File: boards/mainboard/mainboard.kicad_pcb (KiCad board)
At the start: 2 copper layers, 316.2 x 120.7 mm, 278 parts, among them J101 Powerboard <-> Mainboard, J102 Temperature & Pressure, J103 Camera board, J201 RTD_31-36, P901 DEBUG, P902 SWD, SW101 SW_PUSH, SW102 SW_PUSH, SW901 RESET, SW902 BOOT0, U1001 SST26VF064B, U101 LM1117-3.3, U1101 SST26VF064B, U1201 Heat probe encoder, U1202 DS26LV32AT, U1203 DS26LV32AT, U201 RTD_20-30, U202 RTD_1-19, U301 LTC2984, U401 LTC2984, U501 LTC2984, U601 LTC2984, U701 LTC2984, U801 LTC2984, U901 STM32F429ZITx, X901 XO53

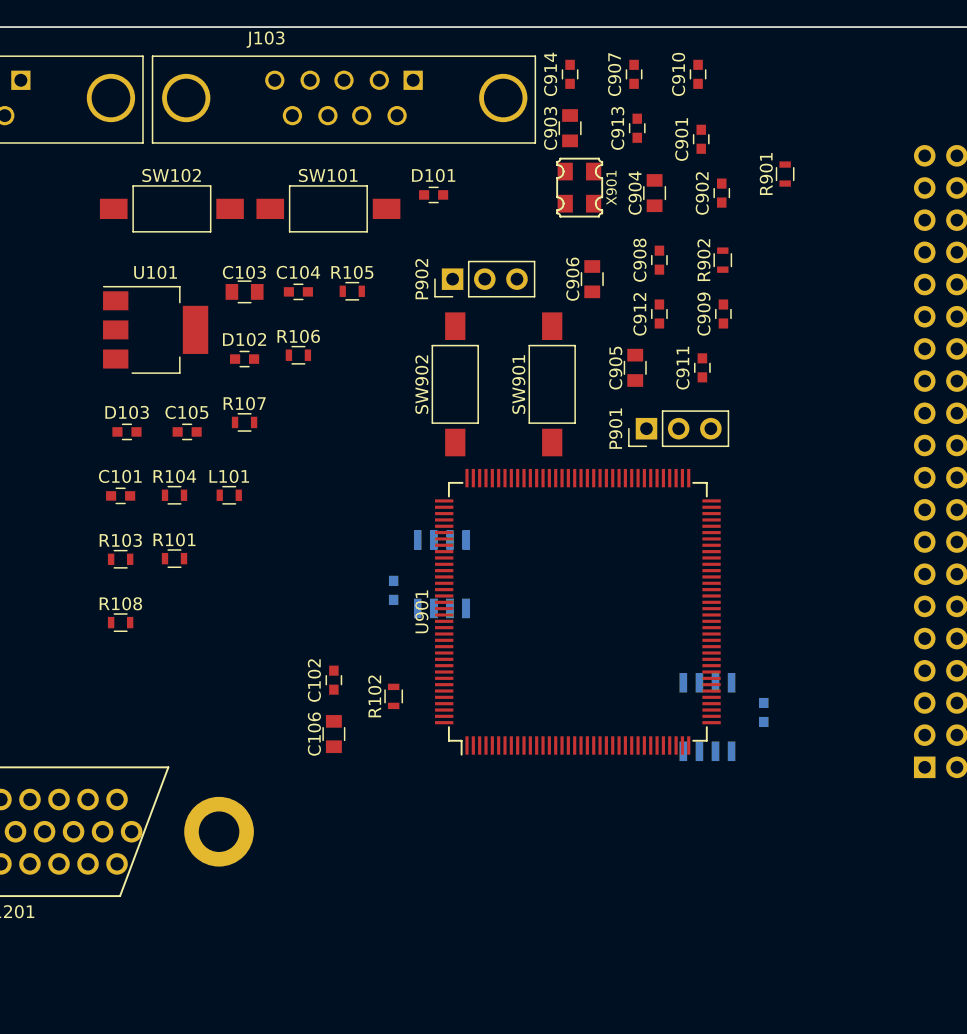
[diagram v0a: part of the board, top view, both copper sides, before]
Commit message: [mainboard] add more local net labels, add not-connected flags
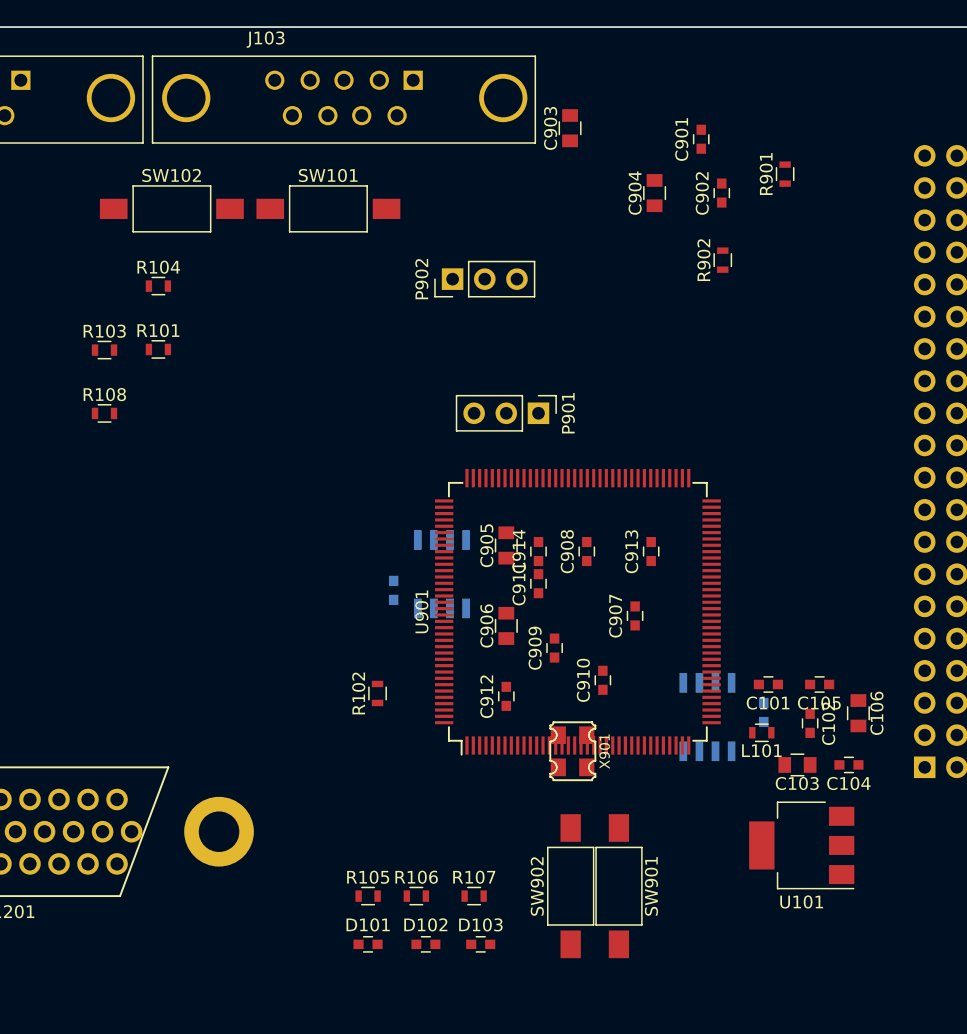
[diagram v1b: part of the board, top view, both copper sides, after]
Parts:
- moved U101 65.2 mm to (88.1, 114.1), turned to 180 degrees
- moved D101 59.4 mm to (53.9, 121.9)
- moved C103 57.4 mm to (87.7, 107.8), turned to 180 degrees
- moved C104 57.3 mm to (91.8, 107.8), turned to 180 degrees
- moved C105 53.7 mm to (89.5, 101.4), turned to 180 degrees
- moved C101 53.2 mm to (85.5, 101.4), turned to 180 degrees
- moved D103 49.1 mm to (62.8, 121.9)
- moved C910 48.4 mm to (72.4, 101.1)
- moved D102 48.4 mm to (58.4, 121.9)
- moved R105 47.7 mm to (53.9, 118.1)
- moved L101 46.0 mm to (84.9, 105.2), turned to 180 degrees
- moved X901 44.5 mm to (70.0, 106.7)
- moved R106 43.7 mm to (57.7, 118.1)
- moved C907 42.7 mm to (74.9, 96.0)
- moved R107 41.5 mm to (62.2, 118.1)
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
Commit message: [mainboard] layout: footprint placement
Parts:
- added C915: 100n, Capacitors_SMD:C_0603, F.Cu at (58.4, 92.2)
- added C916: 100n, Capacitors_SMD:C_0603, F.Cu at (58.4, 97.3)
- added REF**: MountingHole_3.2mm_M3_Pad_Via, Mounting_Holes:MountingHole_3.2mm_M3_Pad_Via, F.Cu at (50.9, 82.5)
- added REF**: MountingHole_3.2mm_M3_Pad_Via, Mounting_Holes:MountingHole_3.2mm_M3_Pad_Via, F.Cu at (1.27, 114.3)
- added REF**: MountingHole_3.2mm_M3_Pad_Via, Mounting_Holes:MountingHole_3.2mm_M3_Pad_Via, F.Cu at (1.27, 53.3)
- added REF**: MountingHole_3.2mm_M3_Pad_Via, Mounting_Holes:MountingHole_3.2mm_M3_Pad_Via, F.Cu at (99.1, 53.3)
- added REF**: MountingHole_3.2mm_M3_Pad_Via, Mounting_Holes:MountingHole_3.2mm_M3_Pad_Via, F.Cu at (99.1, 114.3)
- C902, R101, R102, R103, R104, R108: moved to B.Cu
- moved D101 79.9 mm to (94.0, 52.8), turned to 270 degrees
- moved D102 77.1 mm to (92.7, 52.8), turned to 270 degrees
- moved D103 74.8 mm to (91.4, 52.8), turned to 270 degrees
- moved R105 74.5 mm to (94.0, 55.4), turned to 270 degrees
- moved R106 71.9 mm to (92.7, 55.4), turned to 270 degrees
- moved R107 69.2 mm to (91.4, 55.4), turned to 270 degrees
- moved C901 57.8 mm to (71.6, 115.6), turned to 0 degrees
- moved R901 54.4 mm to (55.9, 105.9), turned to 270 degrees
- moved C902 51.6 mm to (58.4, 108.7), turned to 270 degrees
- moved SW102 49.8 mm to (87.6, 56.7), turned to 90 degrees
- moved R108 47.4 mm to (70.4, 50.8)
- moved R902 45.5 mm to (53.3, 103.4)
- moved J102 45.3 mm to (71.2, 60.8)
- moved R102 45.3 mm to (66.6, 58.4), turned to 0 degrees
- moved R103 35.3 mm to (64.2, 58.4), turned to 180 degrees
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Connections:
- net /Mainboard_Temp_Sensors/Mainboard_LTC2984_1/RTD1_B renamed /Mainboard_Temp_Sensors/T1_RTD1_B
- net /Mainboard_Temp_Sensors/Mainboard_LTC2984_1/RTD1_C renamed /Mainboard_Temp_Sensors/T1_RTD1_C
- net /Mainboard_Temp_Sensors/Mainboard_LTC2984_1/RTD1_D renamed /Mainboard_Temp_Sensors/T1_RTD1_D
- net /Mainboard_Temp_Sensors/Mainboard_LTC2984_1/RTD2_B renamed /Mainboard_Temp_Sensors/T1_RTD2_B
- net /Mainboard_Temp_Sensors/Mainboard_LTC2984_1/RTD2_C renamed /Mainboard_Temp_Sensors/T1_RTD2_C
- net /Mainboard_Temp_Sensors/Mainboard_LTC2984_1/RTD2_D renamed /Mainboard_Temp_Sensors/T1_RTD2_D
- net /Mainboard_Temp_Sensors/Mainboard_LTC2984_1/RTD3_B renamed /Mainboard_Temp_Sensors/T1_RTD3_B
- net /Mainboard_Temp_Sensors/Mainboard_LTC2984_1/RTD3_C renamed /Mainboard_Temp_Sensors/T1_RTD3_C
- net /Mainboard_Temp_Sensors/Mainboard_LTC2984_1/RTD3_D renamed /Mainboard_Temp_Sensors/T1_RTD3_D
- net /Mainboard_Temp_Sensors/Mainboard_LTC2984_1/RTD4_B renamed /Mainboard_Temp_Sensors/T1_RTD4_B
- net /Mainboard_Temp_Sensors/Mainboard_LTC2984_1/RTD4_C renamed /Mainboard_Temp_Sensors/T1_RTD4_C
- net /Mainboard_Temp_Sensors/Mainboard_LTC2984_1/RTD4_D renamed /Mainboard_Temp_Sensors/T1_RTD4_D
- net /Mainboard_Temp_Sensors/Mainboard_LTC2984_1/RTD5_B renamed /Mainboard_Temp_Sensors/T1_RTD5_B
- net /Mainboard_Temp_Sensors/Mainboard_LTC2984_1/RTD5_C renamed /Mainboard_Temp_Sensors/T1_RTD5_C
- net /Mainboard_Temp_Sensors/Mainboard_LTC2984_1/RTD5_D renamed /Mainboard_Temp_Sensors/T1_RTD5_D
- net /Mainboard_Temp_Sensors/Mainboard_LTC2984_1/RTD6_B renamed /Mainboard_Temp_Sensors/T1_RTD6_B
- net /Mainboard_Temp_Sensors/Mainboard_LTC2984_1/RTD6_C renamed /Mainboard_Temp_Sensors/T1_RTD6_C
- net /Mainboard_Temp_Sensors/Mainboard_LTC2984_1/RTD6_D renamed /Mainboard_Temp_Sensors/T1_RTD6_D
- net /Mainboard_Temp_Sensors/Mainboard_LTC2984_1/RTD__A renamed /Mainboard_Temp_Sensors/T1_RTD1_A
- net /Mainboard_Temp_Sensors/Mainboard_LTC2984_2/RTD1_B renamed /Mainboard_Temp_Sensors/T2_RTD1_B
- net /Mainboard_Temp_Sensors/Mainboard_LTC2984_2/RTD1_C renamed /Mainboard_Temp_Sensors/T2_RTD1_C
- net /Mainboard_Temp_Sensors/Mainboard_LTC2984_2/RTD1_D renamed /Mainboard_Temp_Sensors/T2_RTD1_D
- net /Mainboard_Temp_Sensors/Mainboard_LTC2984_2/RTD2_B renamed /Mainboard_Temp_Sensors/T2_RTD2_B
- net /Mainboard_Temp_Sensors/Mainboard_LTC2984_2/RTD2_C renamed /Mainboard_Temp_Sensors/T2_RTD2_C
- net /Mainboard_Temp_Sensors/Mainboard_LTC2984_2/RTD2_D renamed /Mainboard_Temp_Sensors/T2_RTD2_D
- net /Mainboard_Temp_Sensors/Mainboard_LTC2984_2/RTD3_B renamed /Mainboard_Temp_Sensors/T2_RTD3_B
- net /Mainboard_Temp_Sensors/Mainboard_LTC2984_2/RTD3_C renamed /Mainboard_Temp_Sensors/T2_RTD3_C
- net /Mainboard_Temp_Sensors/Mainboard_LTC2984_2/RTD3_D renamed /Mainboard_Temp_Sensors/T2_RTD3_D
- net /Mainboard_Temp_Sensors/Mainboard_LTC2984_2/RTD4_B renamed /Mainboard_Temp_Sensors/T2_RTD4_B
- net /Mainboard_Temp_Sensors/Mainboard_LTC2984_2/RTD4_C renamed /Mainboard_Temp_Sensors/T2_RTD4_C
- net /Mainboard_Temp_Sensors/Mainboard_LTC2984_2/RTD4_D renamed /Mainboard_Temp_Sensors/T2_RTD4_D
- net /Mainboard_Temp_Sensors/Mainboard_LTC2984_2/RTD5_B renamed /Mainboard_Temp_Sensors/T2_RTD5_B
- net /Mainboard_Temp_Sensors/Mainboard_LTC2984_2/RTD5_C renamed /Mainboard_Temp_Sensors/T2_RTD5_C
- net /Mainboard_Temp_Sensors/Mainboard_LTC2984_2/RTD5_D renamed /Mainboard_Temp_Sensors/T2_RTD5_D
- net /Mainboard_Temp_Sensors/Mainboard_LTC2984_2/RTD6_B renamed /Mainboard_Temp_Sensors/T2_RTD6_B
- net /Mainboard_Temp_Sensors/Mainboard_LTC2984_2/RTD6_C renamed /Mainboard_Temp_Sensors/T2_RTD6_C
- net /Mainboard_Temp_Sensors/Mainboard_LTC2984_2/RTD6_D renamed /Mainboard_Temp_Sensors/T2_RTD6_D
- net /Mainboard_Temp_Sensors/Mainboard_LTC2984_2/RTD__A renamed /Mainboard_Temp_Sensors/T2_RTD1_A
- net /Mainboard_Temp_Sensors/Mainboard_LTC2984_3/RTD1_B renamed /Mainboard_Temp_Sensors/T3_RTD1_B
- net /Mainboard_Temp_Sensors/Mainboard_LTC2984_3/RTD1_C renamed /Mainboard_Temp_Sensors/T3_RTD1_C
- net /Mainboard_Temp_Sensors/Mainboard_LTC2984_3/RTD1_D renamed /Mainboard_Temp_Sensors/T3_RTD1_D
- net /Mainboard_Temp_Sensors/Mainboard_LTC2984_3/RTD2_B renamed /Mainboard_Temp_Sensors/T3_RTD2_B
- net /Mainboard_Temp_Sensors/Mainboard_LTC2984_3/RTD2_C renamed /Mainboard_Temp_Sensors/T3_RTD2_C
- net /Mainboard_Temp_Sensors/Mainboard_LTC2984_3/RTD2_D renamed /Mainboard_Temp_Sensors/T3_RTD2_D
- net /Mainboard_Temp_Sensors/Mainboard_LTC2984_3/RTD3_B renamed /Mainboard_Temp_Sensors/T3_RTD3_B
- net /Mainboard_Temp_Sensors/Mainboard_LTC2984_3/RTD3_C renamed /Mainboard_Temp_Sensors/T3_RTD3_C
- net /Mainboard_Temp_Sensors/Mainboard_LTC2984_3/RTD3_D renamed /Mainboard_Temp_Sensors/T3_RTD3_D
- net /Mainboard_Temp_Sensors/Mainboard_LTC2984_3/RTD4_B renamed /Mainboard_Temp_Sensors/T3_RTD4_B
- net /Mainboard_Temp_Sensors/Mainboard_LTC2984_3/RTD4_C renamed /Mainboard_Temp_Sensors/T3_RTD4_C
- net /Mainboard_Temp_Sensors/Mainboard_LTC2984_3/RTD4_D renamed /Mainboard_Temp_Sensors/T3_RTD4_D
- net /Mainboard_Temp_Sensors/Mainboard_LTC2984_3/RTD5_B renamed /Mainboard_Temp_Sensors/T3_RTD5_B
- net /Mainboard_Temp_Sensors/Mainboard_LTC2984_3/RTD5_C renamed /Mainboard_Temp_Sensors/T3_RTD5_C
- net /Mainboard_Temp_Sensors/Mainboard_LTC2984_3/RTD5_D renamed /Mainboard_Temp_Sensors/T3_RTD5_D
- net /Mainboard_Temp_Sensors/Mainboard_LTC2984_3/RTD6_B renamed /Mainboard_Temp_Sensors/T3_RTD6_B
- net /Mainboard_Temp_Sensors/Mainboard_LTC2984_3/RTD6_C renamed /Mainboard_Temp_Sensors/T3_RTD6_C
- net /Mainboard_Temp_Sensors/Mainboard_LTC2984_3/RTD6_D renamed /Mainboard_Temp_Sensors/T3_RTD6_D
- net /Mainboard_Temp_Sensors/Mainboard_LTC2984_3/RTD__A renamed /Mainboard_Temp_Sensors/T3_RTD1_A
- net /Mainboard_Temp_Sensors/Mainboard_LTC2984_4/RTD1_B renamed /Mainboard_Temp_Sensors/T4_RTD1_B
- net /Mainboard_Temp_Sensors/Mainboard_LTC2984_4/RTD1_C renamed /Mainboard_Temp_Sensors/T4_RTD1_C
- net /Mainboard_Temp_Sensors/Mainboard_LTC2984_4/RTD1_D renamed /Mainboard_Temp_Sensors/T4_RTD1_D
- net /Mainboard_Temp_Sensors/Mainboard_LTC2984_4/RTD2_B renamed /Mainboard_Temp_Sensors/T4_RTD2_B
- net /Mainboard_Temp_Sensors/Mainboard_LTC2984_4/RTD2_C renamed /Mainboard_Temp_Sensors/T4_RTD2_C
- net /Mainboard_Temp_Sensors/Mainboard_LTC2984_4/RTD2_D renamed /Mainboard_Temp_Sensors/T4_RTD2_D
- net /Mainboard_Temp_Sensors/Mainboard_LTC2984_4/RTD3_B renamed /Mainboard_Temp_Sensors/T4_RTD3_B
- net /Mainboard_Temp_Sensors/Mainboard_LTC2984_4/RTD3_C renamed /Mainboard_Temp_Sensors/T4_RTD3_C
- net /Mainboard_Temp_Sensors/Mainboard_LTC2984_4/RTD3_D renamed /Mainboard_Temp_Sensors/T4_RTD3_D
- net /Mainboard_Temp_Sensors/Mainboard_LTC2984_4/RTD4_B renamed /Mainboard_Temp_Sensors/T4_RTD4_B
- net /Mainboard_Temp_Sensors/Mainboard_LTC2984_4/RTD4_C renamed /Mainboard_Temp_Sensors/T4_RTD4_C
- net /Mainboard_Temp_Sensors/Mainboard_LTC2984_4/RTD4_D renamed /Mainboard_Temp_Sensors/T4_RTD4_D
- net /Mainboard_Temp_Sensors/Mainboard_LTC2984_4/RTD5_B renamed /Mainboard_Temp_Sensors/T4_RTD5_B
- net /Mainboard_Temp_Sensors/Mainboard_LTC2984_4/RTD5_C renamed /Mainboard_Temp_Sensors/T4_RTD5_C
- net /Mainboard_Temp_Sensors/Mainboard_LTC2984_4/RTD5_D renamed /Mainboard_Temp_Sensors/T4_RTD5_D
- net /Mainboard_Temp_Sensors/Mainboard_LTC2984_4/RTD6_B renamed /Mainboard_Temp_Sensors/T4_RTD6_B
- net /Mainboard_Temp_Sensors/Mainboard_LTC2984_4/RTD6_C renamed /Mainboard_Temp_Sensors/T4_RTD6_C
- net /Mainboard_Temp_Sensors/Mainboard_LTC2984_4/RTD6_D renamed /Mainboard_Temp_Sensors/T4_RTD6_D
- net /Mainboard_Temp_Sensors/Mainboard_LTC2984_4/RTD__A renamed /Mainboard_Temp_Sensors/T4_RTD1_A
- net /Mainboard_Temp_Sensors/Mainboard_LTC2984_5/RTD1_B renamed /Mainboard_Temp_Sensors/T5_RTD1_B
- net /Mainboard_Temp_Sensors/Mainboard_LTC2984_5/RTD1_C renamed /Mainboard_Temp_Sensors/T5_RTD1_C
- net /Mainboard_Temp_Sensors/Mainboard_LTC2984_5/RTD1_D renamed /Mainboard_Temp_Sensors/T5_RTD1_D
- net /Mainboard_Temp_Sensors/Mainboard_LTC2984_5/RTD2_B renamed /Mainboard_Temp_Sensors/T5_RTD2_B
- net /Mainboard_Temp_Sensors/Mainboard_LTC2984_5/RTD2_C renamed /Mainboard_Temp_Sensors/T5_RTD2_C
- net /Mainboard_Temp_Sensors/Mainboard_LTC2984_5/RTD2_D renamed /Mainboard_Temp_Sensors/T5_RTD2_D
- net /Mainboard_Temp_Sensors/Mainboard_LTC2984_5/RTD3_B renamed /Mainboard_Temp_Sensors/T5_RTD3_B
- net /Mainboard_Temp_Sensors/Mainboard_LTC2984_5/RTD3_C renamed /Mainboard_Temp_Sensors/T5_RTD3_C
- net /Mainboard_Temp_Sensors/Mainboard_LTC2984_5/RTD3_D renamed /Mainboard_Temp_Sensors/T5_RTD3_D
- net /Mainboard_Temp_Sensors/Mainboard_LTC2984_5/RTD4_B renamed /Mainboard_Temp_Sensors/T5_RTD4_B
- net /Mainboard_Temp_Sensors/Mainboard_LTC2984_5/RTD4_C renamed /Mainboard_Temp_Sensors/T5_RTD4_C
- net /Mainboard_Temp_Sensors/Mainboard_LTC2984_5/RTD4_D renamed /Mainboard_Temp_Sensors/T5_RTD4_D
- net /Mainboard_Temp_Sensors/Mainboard_LTC2984_5/RTD5_B renamed /Mainboard_Temp_Sensors/T5_RTD5_B
- net /Mainboard_Temp_Sensors/Mainboard_LTC2984_5/RTD5_C renamed /Mainboard_Temp_Sensors/T5_RTD5_C
- net /Mainboard_Temp_Sensors/Mainboard_LTC2984_5/RTD5_D renamed /Mainboard_Temp_Sensors/T5_RTD5_D
- net /Mainboard_Temp_Sensors/Mainboard_LTC2984_5/RTD6_B renamed /Mainboard_Temp_Sensors/T5_RTD6_B
- net /Mainboard_Temp_Sensors/Mainboard_LTC2984_5/RTD6_C renamed /Mainboard_Temp_Sensors/T5_RTD6_C
- net /Mainboard_Temp_Sensors/Mainboard_LTC2984_5/RTD6_D renamed /Mainboard_Temp_Sensors/T5_RTD6_D
- net /Mainboard_Temp_Sensors/Mainboard_LTC2984_5/RTD__A renamed /Mainboard_Temp_Sensors/T5_RTD1_A
- net /Mainboard_Temp_Sensors/Mainboard_LTC2984_6/RTD1_B renamed /Mainboard_Temp_Sensors/T6_RTD1_B
- net /Mainboard_Temp_Sensors/Mainboard_LTC2984_6/RTD1_C renamed /Mainboard_Temp_Sensors/T6_RTD1_C
- net /Mainboard_Temp_Sensors/Mainboard_LTC2984_6/RTD1_D renamed /Mainboard_Temp_Sensors/T6_RTD1_D
- net /Mainboard_Temp_Sensors/Mainboard_LTC2984_6/RTD2_B renamed /Mainboard_Temp_Sensors/T6_RTD2_B
- net /Mainboard_Temp_Sensors/Mainboard_LTC2984_6/RTD2_C renamed /Mainboard_Temp_Sensors/T6_RTD2_C
- net /Mainboard_Temp_Sensors/Mainboard_LTC2984_6/RTD2_D renamed /Mainboard_Temp_Sensors/T6_RTD2_D
- net /Mainboard_Temp_Sensors/Mainboard_LTC2984_6/RTD3_B renamed /Mainboard_Temp_Sensors/T6_RTD3_B
- net /Mainboard_Temp_Sensors/Mainboard_LTC2984_6/RTD3_C renamed /Mainboard_Temp_Sensors/T6_RTD3_C
- net /Mainboard_Temp_Sensors/Mainboard_LTC2984_6/RTD3_D renamed /Mainboard_Temp_Sensors/T6_RTD3_D
- net /Mainboard_Temp_Sensors/Mainboard_LTC2984_6/RTD4_B renamed /Mainboard_Temp_Sensors/T6_RTD4_B
- net /Mainboard_Temp_Sensors/Mainboard_LTC2984_6/RTD4_C renamed /Mainboard_Temp_Sensors/T6_RTD4_C
- net /Mainboard_Temp_Sensors/Mainboard_LTC2984_6/RTD4_D renamed /Mainboard_Temp_Sensors/T6_RTD4_D
- net /Mainboard_Temp_Sensors/Mainboard_LTC2984_6/RTD5_B renamed /Mainboard_Temp_Sensors/T6_RTD5_B
- net /Mainboard_Temp_Sensors/Mainboard_LTC2984_6/RTD5_C renamed /Mainboard_Temp_Sensors/T6_RTD5_C
- net /Mainboard_Temp_Sensors/Mainboard_LTC2984_6/RTD5_D renamed /Mainboard_Temp_Sensors/T6_RTD5_D
- net /Mainboard_Temp_Sensors/Mainboard_LTC2984_6/RTD6_B renamed /Mainboard_Temp_Sensors/T6_RTD6_B
- net /Mainboard_Temp_Sensors/Mainboard_LTC2984_6/RTD6_C renamed /Mainboard_Temp_Sensors/T6_RTD6_C
- net /Mainboard_Temp_Sensors/Mainboard_LTC2984_6/RTD6_D renamed /Mainboard_Temp_Sensors/T6_RTD6_D
- net /Mainboard_Temp_Sensors/Mainboard_LTC2984_6/RTD__A renamed /Mainboard_Temp_Sensors/T6_RTD1_A
- net Net-(C102-Pad1) renamed /5V_filtered
- net Net-(C902-Pad1) renamed /Mainboard microcontroller/NRST
- net Net-(D101-Pad2) renamed /LED1_R
- net Net-(D102-Pad2) renamed /LED3_R
- net Net-(D103-Pad2) renamed /LED2_R
- net Net-(J103-Pad6) renamed /CAM_GND
- net Net-(R902-Pad1) renamed /Mainboard microcontroller/BOOT0
- J103 pad 3: Net-(J103-Pad3) -> (no net)
- J103 pad 4: Net-(J103-Pad4) -> (no net)
- J103 pad 5: Net-(J103-Pad5) -> (no net)
- J103 pad 7: Net-(J103-Pad7) -> (no net)
- J103 pad 8: Net-(J103-Pad8) -> (no net)
- J103 pad 9: Net-(J103-Pad9) -> (no net)
- U1203 pad 10: Net-(U1203-Pad10) -> (no net)
- U1203 pad 11: Net-(U1203-Pad11) -> (no net)
- U1203 pad 13: Net-(U1203-Pad13) -> (no net)
- U1203 pad 14: Net-(U1203-Pad14) -> (no net)
- U1203 pad 15: Net-(U1203-Pad15) -> (no net)
- U1203 pad 9: Net-(U1203-Pad9) -> (no net)
- U202 pad 20: Net-(U202-Pad20) -> (no net)
- U202 pad 59: Net-(U202-Pad59) -> (no net)
- U301 pad 10: Net-(U301-Pad10) -> (no net)
- U401 pad 10: Net-(U401-Pad10) -> (no net)
- U501 pad 10: Net-(U501-Pad10) -> (no net)
- U601 pad 10: Net-(U601-Pad10) -> (no net)
- U701 pad 10: Net-(U701-Pad10) -> (no net)
- U801 pad 10: Net-(U801-Pad10) -> (no net)
- U901 pad 100: Net-(U901-Pad100) -> (no net)
- U901 pad 103: Net-(U901-Pad103) -> (no net)
- U901 pad 104: Net-(U901-Pad104) -> (no net)
- U901 pad 114: Net-(U901-Pad114) -> (no net)
- U901 pad 115: Net-(U901-Pad115) -> (no net)
- U901 pad 117: Net-(U901-Pad117) -> (no net)
- U901 pad 118: Net-(U901-Pad118) -> (no net)
- U901 pad 119: Net-(U901-Pad119) -> (no net)
- U901 pad 124: Net-(U901-Pad124) -> (no net)
- U901 pad 132: Net-(U901-Pad132) -> (no net)
- U901 pad 2: Net-(U901-Pad2) -> (no net)
- U901 pad 23: Net-(U901-Pad23) -> /Mainboard microcontroller/OSC_8MHz
- U901 pad 3: Net-(U901-Pad3) -> (no net)
- U901 pad 32: Net-(U901-Pad32) -> (no net)
- U901 pad 37: Net-(U901-Pad37) -> (no net)
- U901 pad 45: Net-(U901-Pad45) -> (no net)
- U901 pad 46: Net-(U901-Pad46) -> (no net)
- U901 pad 47: Net-(U901-Pad47) -> (no net)
- U901 pad 48: Net-(U901-Pad48) -> (no net)
- U901 pad 49: Net-(U901-Pad49) -> (no net)
- U901 pad 50: Net-(U901-Pad50) -> (no net)
- U901 pad 53: Net-(U901-Pad53) -> (no net)
- U901 pad 54: Net-(U901-Pad54) -> (no net)
- U901 pad 55: Net-(U901-Pad55) -> (no net)
- U901 pad 56: Net-(U901-Pad56) -> (no net)
- U901 pad 57: Net-(U901-Pad57) -> (no net)
- U901 pad 58: Net-(U901-Pad58) -> (no net)
- U901 pad 67: Net-(U901-Pad67) -> (no net)
- U901 pad 68: Net-(U901-Pad68) -> (no net)
- U901 pad 70: Net-(U901-Pad70) -> (no net)
- U901 pad 73: Net-(U901-Pad73) -> (no net)
- U901 pad 74: Net-(U901-Pad74) -> (no net)
- U901 pad 80: Net-(U901-Pad80) -> (no net)
- U901 pad 85: Net-(U901-Pad85) -> (no net)
- U901 pad 90: Net-(U901-Pad90) -> (no net)
- U901 pad 91: Net-(U901-Pad91) -> (no net)
- U901 pad 92: Net-(U901-Pad92) -> (no net)
- U901 pad 93: Net-(U901-Pad93) -> (no net)
- U901 pad 99: Net-(U901-Pad99) -> (no net)
- X901 pad 1: Net-(X901-Pad1) -> (no net)
- X901 pad 3: (no net) -> /Mainboard microcontroller/OSC_8MHz
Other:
- board size 316.2 x 120.7 mm -> 105.4 x 68.6 mm

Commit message: [mainboard] add mounting holes to schematic
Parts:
- removed REF** (x5): MountingHole_3.2mm_M3_Pad_Via, Mounting_Holes:MountingHole_3.2mm_M3_Pad_Via
- added J1001: FL2_CS, Measurement_Points:Measurement_Point_Round-SMD-Pad_Small, F.Cu at (123.2, 81.3)
- added J1002: FL2_SCK, Measurement_Points:Measurement_Point_Round-SMD-Pad_Small, F.Cu at (120.7, 81.3)
- added J1003: FL2_MISO, Measurement_Points:Measurement_Point_Round-SMD-Pad_Small, F.Cu at (119.4, 83.8)
- added J1004: FL2_MOSI, Measurement_Points:Measurement_Point_Round-SMD-Pad_Small, F.Cu at (115.6, 85.1)
- added J104: temp_SCL, Measurement_Points:Measurement_Point_Round-SMD-Pad_Small, F.Cu at (130.8, 86.3)
- added J105: temp_SDA, Measurement_Points:Measurement_Point_Round-SMD-Pad_Small, F.Cu at (123.2, 85.1)
- added J106: pres_SCL, Measurement_Points:Measurement_Point_Round-SMD-Pad_Small, F.Cu at (134.6, 83.8)
- added J107: pres_SDA, Measurement_Points:Measurement_Point_Round-SMD-Pad_Small, F.Cu at (123.2, 87.6)
- added J108: RasPi_TX, Measurement_Points:Measurement_Point_Round-SMD-Pad_Small, F.Cu at (128.3, 87.6)
- added J109: RasPi_RX, Measurement_Points:Measurement_Point_Round-SMD-Pad_Small, F.Cu at (125.7, 83.8)
- added J110: 3V3, Measurement_Points:Measurement_Point_Round-SMD-Pad_Small, F.Cu at (129.5, 83.8)
- added J1101: FL1_CS, Measurement_Points:Measurement_Point_Round-SMD-Pad_Small, F.Cu at (118.1, 85.1)
- added J1102: FL1_SCK, Measurement_Points:Measurement_Point_Round-SMD-Pad_Small, F.Cu at (116.8, 82.5)
- added J1103: FL1_MISO, Measurement_Points:Measurement_Point_Round-SMD-Pad_Small, F.Cu at (118.1, 81.3)
- added J1104: FL1_MOSI, Measurement_Points:Measurement_Point_Round-SMD-Pad_Small, F.Cu at (114.3, 82.5)
- added J111: GND, Measurement_Points:Measurement_Point_Round-SMD-Pad_Small, F.Cu at (120.7, 86.4)
- added J112: M3, Mounting_Holes:MountingHole_3.2mm_M3_Pad_Via, F.Cu at (1.27, 114.3)
- added J113: M3, Mounting_Holes:MountingHole_3.2mm_M3_Pad_Via, F.Cu at (99.1, 53.3)
- added J114: M3, Mounting_Holes:MountingHole_3.2mm_M3_Pad_Via, F.Cu at (99.1, 114.3)
- added J115: M3, Mounting_Holes:MountingHole_3.2mm_M3_Pad_Via, F.Cu at (45.7, 88.9)
- added J116: M3, Mounting_Holes:MountingHole_3.2mm_M3_Pad_Via, F.Cu at (1.27, 53.3)
- added J117: M3, Mounting_Holes:MountingHole_3.2mm_M3_Pad_Via, F.Cu at (-36.8, 85.1)
- added J1201: ENC1_A, Measurement_Points:Measurement_Point_Round-SMD-Pad_Small, F.Cu at (115.6, 81.3)
- added J1202: ENC1_B, Measurement_Points:Measurement_Point_Round-SMD-Pad_Small, F.Cu at (113.0, 85.1)
- added J1203: ENC2_A, Measurement_Points:Measurement_Point_Round-SMD-Pad_Small, F.Cu at (115.6, 87.6)
- added J1204: ENC2_B, Measurement_Points:Measurement_Point_Round-SMD-Pad_Small, F.Cu at (113.0, 87.6)
- added J1205: ENC3_A, Measurement_Points:Measurement_Point_Round-SMD-Pad_Small, F.Cu at (133.3, 86.4)
- added J1206: ENC3_B, Measurement_Points:Measurement_Point_Round-SMD-Pad_Small, F.Cu at (128.3, 85.1)
- added J202: T_SPI1_SCK, Measurement_Points:Measurement_Point_Round-SMD-Pad_Small, F.Cu at (121.9, 82.5)
- added J203: T_SPI1_MISO, Measurement_Points:Measurement_Point_Round-SMD-Pad_Small, F.Cu at (120.7, 85.1)
- added J204: T_SPI1_MOSI, Measurement_Points:Measurement_Point_Round-SMD-Pad_Small, F.Cu at (128.3, 82.5)
- added J205: T_SPI2_SCK, Measurement_Points:Measurement_Point_Round-SMD-Pad_Small, F.Cu at (125.7, 88.9)
- added J206: T_SPI2_MISO, Measurement_Points:Measurement_Point_Round-SMD-Pad_Small, F.Cu at (132.1, 85.1)
- added J207: T_SPI2_MOSI, Measurement_Points:Measurement_Point_Round-SMD-Pad_Small, F.Cu at (125.7, 86.4)
- added J208: T_SPI1_CS1, Measurement_Points:Measurement_Point_Round-SMD-Pad_Small, F.Cu at (132.1, 82.5)
- added J209: T_SPI1_CS2, Measurement_Points:Measurement_Point_Round-SMD-Pad_Small, F.Cu at (120.7, 88.9)
- added J210: T_SPI1_CS3, Measurement_Points:Measurement_Point_Round-SMD-Pad_Small, F.Cu at (118.1, 87.6)
- added J211: T_SPI2_CS1, Measurement_Points:Measurement_Point_Round-SMD-Pad_Small, F.Cu at (119.4, 82.5)
- added J212: T_SPI2_CS2, Measurement_Points:Measurement_Point_Round-SMD-Pad_Small, F.Cu at (124.5, 82.5)
- added J213: T_SPI2_CS3, Measurement_Points:Measurement_Point_Round-SMD-Pad_Small, F.Cu at (126.4, 81.3)
- added R109: 0R, Resistors_SMD:R_0603, F.Cu at (-1.79, 111.8)
- added R110: 0R, Resistors_SMD:R_0603, F.Cu at (96.0, 50.8)
- added R111: 0R, Resistors_SMD:R_0603, F.Cu at (95.2, 116.1)
- added R112: 0R, Resistors_SMD:R_0603, F.Cu at (43.7, 86.4)
- added R113: 0R, Resistors_SMD:R_0603, F.Cu at (4.33, 50.8)
- added R114: 0R, Resistors_SMD:R_0603, F.Cu at (-38.9, 82.5)
- D101, D102, D103: footprint Capacitors_SMD:C_0603 -> LEDs:LED_0603
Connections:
- net Net-(R1201-Pad1) renamed /Heat_Probe_Encoder/ENC1_A_filter
- net Net-(R1201-Pad2) renamed /Heat_Probe_Encoder/ENC1_A_+
- net Net-(R1202-Pad1) renamed /Heat_Probe_Encoder/ENC1_B_filter
- net Net-(R1202-Pad2) renamed /Heat_Probe_Encoder/ENC1_B_+
- net Net-(R1203-Pad1) renamed /Heat_Probe_Encoder/ENC2_A_filter
- net Net-(R1203-Pad2) renamed /Heat_Probe_Encoder/ENC2_A_+
- net Net-(R1204-Pad1) renamed /Heat_Probe_Encoder/ENC2_B_filter
- net Net-(R1204-Pad2) renamed /Heat_Probe_Encoder/ENC2_B_+
- net Net-(R1205-Pad1) renamed /Heat_Probe_Encoder/ENC3_A_filter
- net Net-(R1205-Pad2) renamed /Heat_Probe_Encoder/ENC3_A_+
- net Net-(R1206-Pad1) renamed /Heat_Probe_Encoder/ENC3_B_filter
- net Net-(R1206-Pad2) renamed /Heat_Probe_Encoder/ENC3_B_+
- net Net-(U1201-Pad14) renamed /Heat_Probe_Encoder/ENC2_A_-
- net Net-(U1201-Pad17) renamed /Heat_Probe_Encoder/ENC3_B_-
- net Net-(U1201-Pad20) renamed /Heat_Probe_Encoder/ENC1_A_-
- net Net-(U1201-Pad23) renamed /Heat_Probe_Encoder/ENC2_B_-
- net Net-(U1201-Pad3) renamed /Heat_Probe_Encoder/ENC1_B_-
- net Net-(U1201-Pad7) renamed /Heat_Probe_Encoder/ENC3_A_-

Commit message: [mainboard] component placement (wip...)
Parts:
- added C1207: 100n, Capacitors_SMD:C_0603, B.Cu at (56.6, 74.9)
- added C1208: 100n, Capacitors_SMD:C_0603, F.Cu at (59.2, 77.5)
- C1202, C1203, C1204, C1205, C1206, C905, C906, R1201, R1202, R1203, R1204, R1205, R1206, R1207, R1208, R1211, R1212, R1214, R1215, R1216, R1217, R1218, U1202, U1203: moved to B.Cu
- moved R1217 67.6 mm to (77.5, 74.2)
- moved C1206 65.9 mm to (72.4, 71.6), turned to 90 degrees
- moved C1205 63.1 mm to (77.5, 71.6), turned to 90 degrees
- moved C1201 60.3 mm to (57.7, 87.6), turned to 180 degrees
- moved R1218 58.8 mm to (72.4, 74.2)
- moved R1213 57.1 mm to (57.7, 86.4), turned to 180 degrees
- moved R1207 56.3 mm to (56.6, 86.4), turned to 0 degrees
- moved C1203 53.7 mm to (50.8, 92.0), turned to 90 degrees
- moved R1216 52.5 mm to (53.3, 94.5)
- moved R1203 52.5 mm to (52.6, 78.7), turned to 180 degrees
- moved R1214 50.8 mm to (48.3, 94.5)
- moved R1208 49.5 mm to (55.1, 87.6), turned to 180 degrees
- moved R1206 49.2 mm to (52.1, 68.1), turned to 90 degrees
- moved R1202 48.9 mm to (53.9, 86.4), turned to 180 degrees
- moved R1201 48.5 mm to (57.7, 87.6), turned to 0 degrees
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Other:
- board size 105.4 x 68.6 mm -> 100.3 x 68.6 mm

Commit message: [mainboard] component placement, board dimensions 110x70mm2
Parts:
- removed R302, R402, R502: 2k00, Resistors_THT:R_Axial_DIN0204_L3.6mm_D1.6mm_P5.08mm_Horizontal
- C317, C319, C321, C322, C323, C324, C325, C326, C327, C417, C419, C421, C422, C423, C424, C425, C426, C427, C517, C519, C521, C522, C523, C524, C525, C526, C527, D301, D401, D501, J1001, J1002, J1003, J1004, J104, J105, J106, J107, J1101, J1102, J1103, J1104, J1202, J1203, J1204, J1205, J1206, R301, R303, R304, R401, R403, R404, R501, R503, R504, U301, U401, U501: moved to B.Cu
- moved C701 298.3 mm to (-60.5, 73.6)
- moved C702 298.3 mm to (-58.0, 57.6)
- moved C705 298.3 mm to (-57.0, 62.7)
- moved C706 298.3 mm to (-60.5, 68.5)
- moved C708 298.3 mm to (-49.5, 57.6)
- moved C709 298.3 mm to (-53.8, 57.6)
- moved C712 298.3 mm to (-61.3, 63.5)
- moved C714 298.3 mm to (-45.3, 57.6)
- moved C716 298.3 mm to (-61.0, 78.6)
- moved C717 298.3 mm to (-56.3, 67.7)
- moved C718 298.3 mm to (-56.3, 72.8)
- moved C719 298.3 mm to (-52.8, 62.7)
- moved C720 298.3 mm to (-52.0, 67.7)
- moved C721 298.3 mm to (-68.4, 57.6)
- moved C722 298.3 mm to (-79.4, 77.5)
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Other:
- board size 100.3 x 68.6 mm -> 110.5 x 68.6 mm
- rule trace_min: 0.2 -> 0.15

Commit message: [mainboard] semi-final component placement
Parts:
- removed R602, R702, R802: 2k00, Resistors_THT:R_Axial_DIN0204_L3.6mm_D1.6mm_P5.08mm_Horizontal
- C601, C602, C603, C604, C605, C606, C607, C608, C609, C610, C611, C612, C613, C614, C615, C616, C618, C620, C701, C702, C703, C704, C705, C706, C707, C708, C709, C710, C712, C714, C716, C717, C718, C720, C801, C802, C803, C804, C805, C806, C807, C808, C809, C810, C811, C812, C813, C814, C815, C816, C818, C820, J108, J109: moved to B.Cu
- C902: moved to F.Cu
- moved J204 115.3 mm to (24.1, 33.0)
- moved J206 115.3 mm to (27.9, 35.6)
- moved J208 115.3 mm to (27.9, 33.0)
- moved J202 115.3 mm to (17.8, 33.0)
- moved J203 115.3 mm to (16.5, 35.6)
- moved J205 115.3 mm to (21.6, 39.4)
- moved J207 115.3 mm to (21.6, 36.8)
- moved J209 115.3 mm to (16.5, 39.4)
- moved J210 115.3 mm to (14.0, 38.1)
- moved J211 115.3 mm to (15.2, 33.0)
- moved J212 115.3 mm to (20.3, 33.0)
- moved J213 115.3 mm to (22.2, 31.8)
- moved C722 98.1 mm to (18.8, 77.5), turned to 180 degrees
- moved C703 95.1 mm to (24.9, 90.2)
- moved C710 94.3 mm to (24.9, 82.5), turned to 180 degrees
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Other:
- board size 110.5 x 68.6 mm -> 107.3 x 68.6 mm
- rule pad_to_mask_clearance: 0.2 -> 0.075
